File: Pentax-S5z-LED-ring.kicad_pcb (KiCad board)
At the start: 2 copper layers, 41.7 x 41.7 mm, 1 part

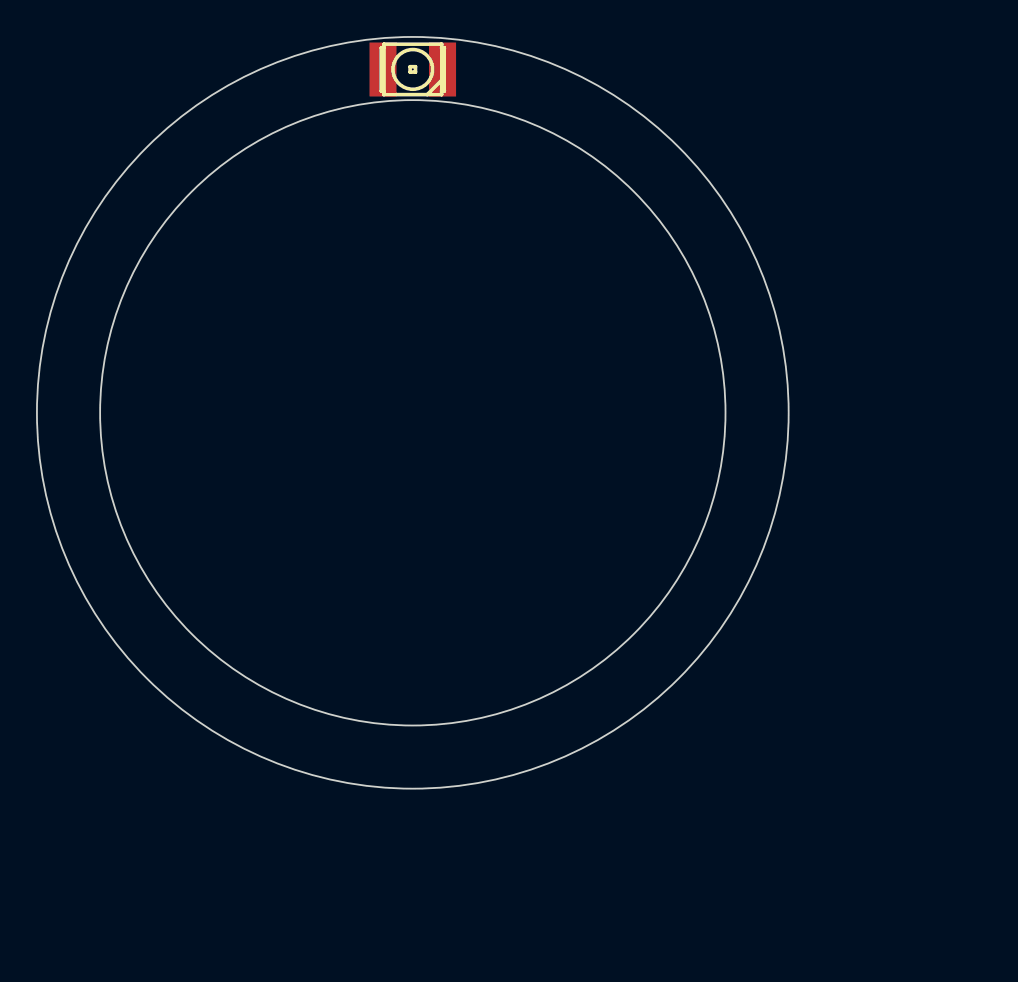
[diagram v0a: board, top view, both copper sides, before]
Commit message: First doodles.
Haven't decided yet how to drive the LEDs. Linear or switch-mode? Maybe
with 2x AAA cells + boost converter + ATtiny13 for PWM control.
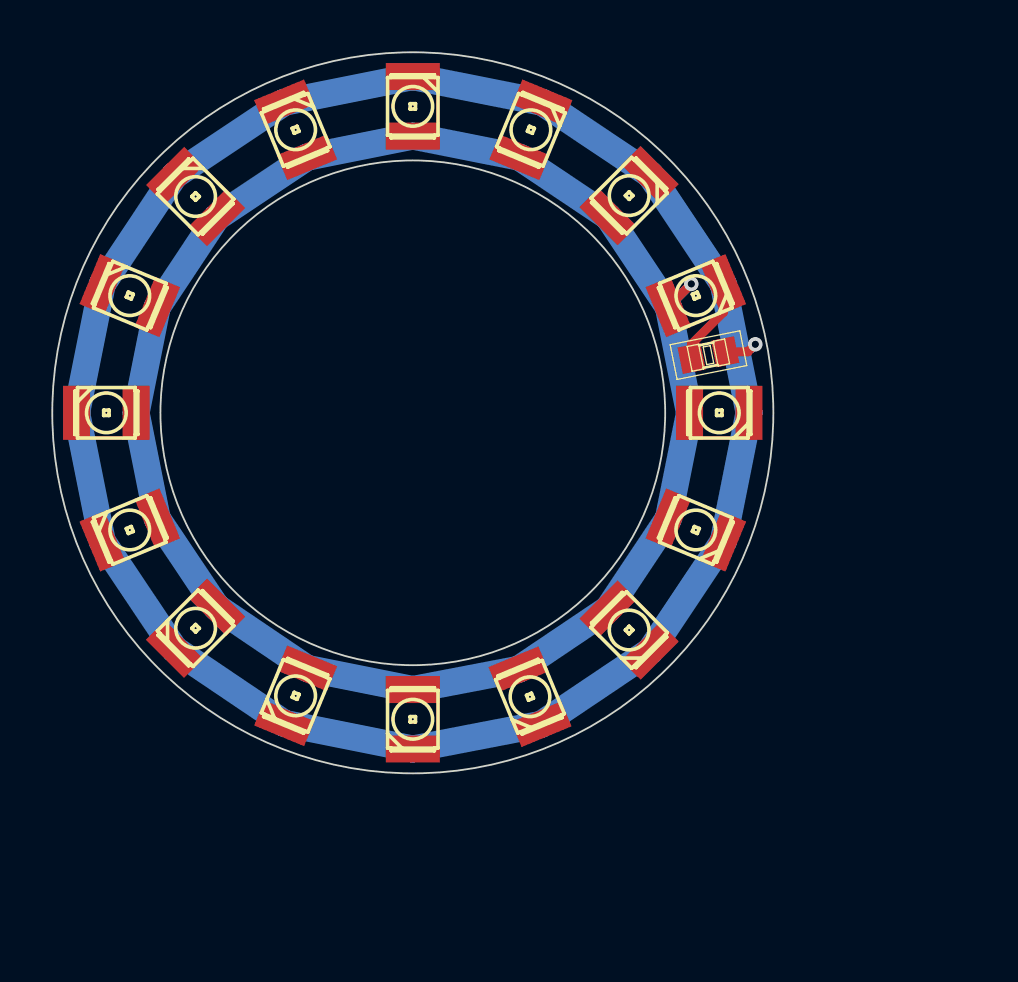
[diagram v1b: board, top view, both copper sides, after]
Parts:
- added >NAME: >VALUE, -R0805, F.Cu at (81.4, 61.8)
- added LED: VAL**, MADW__PLCC2, F.Cu at (80.7, 71.5)
- added LED: VAL**, MADW__PLCC2, F.Cu at (82.0, 65.0)
- added LED: VAL**, MADW__PLCC2, F.Cu at (48.0, 65.0)
- added LED: VAL**, MADW__PLCC2, F.Cu at (77.0, 53.0)
- added LED: VAL**, MADW__PLCC2, F.Cu at (53.0, 53.0)
- added LED: VAL**, MADW__PLCC2, F.Cu at (53.0, 77.0)
- added LED: VAL**, MADW__PLCC2, F.Cu at (77.0, 77.0)
- added LED: VAL**, MADW__PLCC2, F.Cu at (71.5, 49.3)
- added LED: VAL**, MADW__PLCC2, F.Cu at (49.3, 58.5)
- added LED: VAL**, MADW__PLCC2, F.Cu at (49.3, 71.5)
- added LED: VAL**, MADW__PLCC2, F.Cu at (80.7, 58.5)
- added LED: VAL**, MADW__PLCC2, F.Cu at (71.5, 80.8)
- added LED: VAL**, MADW__PLCC2, F.Cu at (58.5, 49.3)
- added LED: VAL**, MADW__PLCC2, F.Cu at (58.5, 80.7)
- added LED: VAL**, MADW__PLCC2, F.Cu at (65.0, 82.0)
- moved LED 2.05 mm to (65.0, 48.0), turned to 90 degrees
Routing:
- net (no net): track 0.00 -> 223.7 mm, vias 0 -> 2
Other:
- board size 41.7 x 41.7 mm -> 40 x 40 mm
- net class Default: clearance 0.254 -> 0.25; trace_width 0.254 -> 0.5; via_dia 0.889 -> 0.8; via_drill 0.635 -> 0.4
- rule pad_to_mask_clearance: 0.2 -> 0
- rule trace_clearance: 0.254 -> 0.25
- rule trace_min: 0.254 -> 0.25
- rule via_min_drill: 0.508 -> 0.4
- rule via_min_size: 0.889 -> 0.8

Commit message: Placed a few traces.
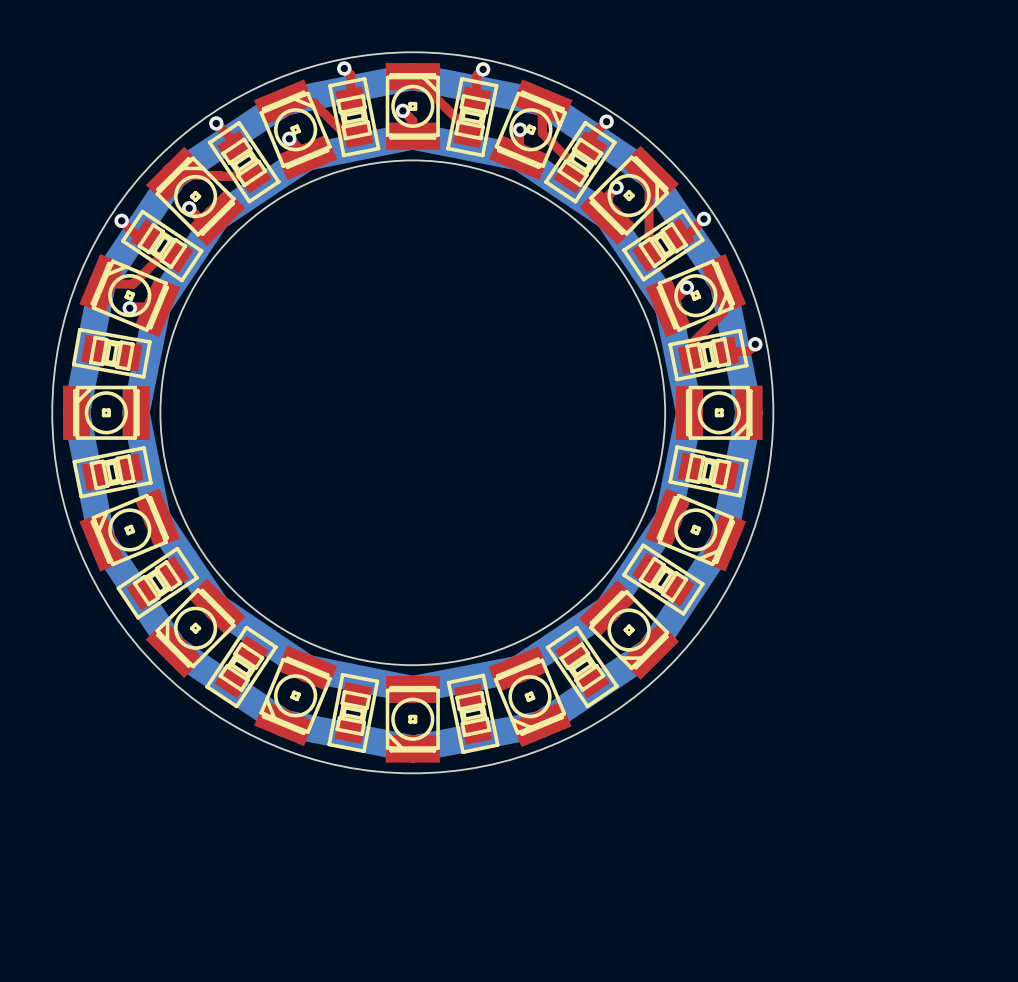
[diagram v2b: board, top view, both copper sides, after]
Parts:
- removed LED: VAL**, MADW__PLCC2
- added D3: LED, MADW__PLCC2-3528, F.Cu at (77.0, 53.0)
- added R1: 10R, MADW__R0805, F.Cu at (68.3, 48.6)
- added R10: 10R, MADW__R0805, F.Cu at (55.5, 79.1)
- added R11: 10R, MADW__R0805, F.Cu at (50.9, 74.5)
- added R12: 10R, MADW__R0805, F.Cu at (48.4, 68.3)
- added R13: 10R, MADW__R0805, F.Cu at (48.3, 61.7)
- added R14: 10R, MADW__R0805, F.Cu at (51.1, 55.8)
- added R15: 10R, MADW__R0805, F.Cu at (55.6, 51.1)
- added R16: 10R, MADW__R0805, F.Cu at (61.8, 48.6)
- added R2: 10R, MADW__R0805, F.Cu at (74.3, 51.1)
- added R3: 10R, MADW__R0805, F.Cu at (78.9, 55.7)
- added R5: 10R, MADW__R0805, F.Cu at (81.4, 68.2)
- added R6: 10R, MADW__R0805, F.Cu at (78.9, 74.2)
- added R7: 10R, MADW__R0805, F.Cu at (74.4, 79.1)
- added R8: 10R, MADW__R0805, F.Cu at (68.3, 81.7)
- added R9: 10R, MADW__R0805, F.Cu at (61.7, 81.7)
- D1, D2, D4, D5, D6, D7: renamed from LED; value VAL** -> LED; footprint MADW__PLCC2 -> MADW__PLCC2-3528
- D10, D11, D12, D13, D14, D15, D16, D8, D9: renamed from LED; value VAL** -> LED
- R4: renamed from >NAME; value >VALUE -> 10R; footprint -R0805 -> MADW__R0805
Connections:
- D1 pad 1: (no net) -> N-0000018
- D1 pad 2: (no net) -> N-000002
- D10 pad 1: (no net) -> N-0000018
- D10 pad 2: (no net) -> N-0000010
- D11 pad 1: (no net) -> N-0000018
- D11 pad 2: (no net) -> N-0000011
- D12 pad 1: (no net) -> N-0000018
- D12 pad 2: (no net) -> N-0000012
- D13 pad 1: (no net) -> N-0000018
- D13 pad 2: (no net) -> N-0000013
- D14 pad 1: (no net) -> N-0000018
- D14 pad 2: (no net) -> N-0000014
- D15 pad 1: (no net) -> N-0000018
- D15 pad 2: (no net) -> N-0000015
- D16 pad 1: (no net) -> N-0000018
- D16 pad 2: (no net) -> N-0000016
- D2 pad 1: (no net) -> N-0000018
- D2 pad 2: (no net) -> N-000003
- D4 pad 1: (no net) -> N-0000018
- D4 pad 2: (no net) -> N-000001
- D5 pad 1: (no net) -> N-0000018
- D5 pad 2: (no net) -> N-000005
- D6 pad 1: (no net) -> N-0000018
- D6 pad 2: (no net) -> N-000006
- D7 pad 1: (no net) -> N-0000018
- D7 pad 2: (no net) -> N-000007
- D8 pad 1: (no net) -> N-0000018
- D8 pad 2: (no net) -> N-000008
- D9 pad 1: (no net) -> N-0000018
- D9 pad 2: (no net) -> N-000009
- R4 pad 1: (no net) -> N-000001
- R4 pad 2: (no net) -> N-0000017
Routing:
- net (no net): track 223.7 -> 0.00 mm, vias 2 -> 0
- net N-0000017: track 0.00 -> 137.3 mm, vias 0 -> 7
- net N-0000018: track 0.00 -> 118.2 mm, vias 0 -> 7
- net N-000001: track 0.00 -> 4.84 mm
- net N-0000016: track 0.00 -> 4.79 mm
- net N-000003: track 0.00 -> 4.77 mm
- net N-0000014: track 0.00 -> 4.77 mm
- net N-000004: track 0.00 -> 4.47 mm
- net N-0000015: track 0.00 -> 4.42 mm
- net N-000002: track 0.00 -> 4.36 mm

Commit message: Tweaks.
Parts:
- moved R11 0.32 mm to (51.1, 74.2), turned to 213.9 degrees
- moved R8 0.32 mm to (68.2, 81.4), turned to 281.7 degrees
- moved R13 0.30 mm to (48.6, 61.8)
- moved R10 0.28 mm to (55.7, 78.9), turned to 236.5 degrees
- moved R12 0.25 mm to (48.6, 68.2), turned to 191.3 degrees
- moved R9 0.25 mm to (61.8, 81.4), turned to 259.1 degrees
- moved R7 0.11 mm to (74.3, 79.0), turned to 304.3 degrees
- turned R6 to 326.9 degrees
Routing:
- net N-0000018: track 118.2 -> 148.4 mm, vias 7 -> 16
- net N-0000017: track 137.3 -> 163.4 mm, vias 7 -> 16
- net N-000009: track 0.00 -> 4.71 mm
- net N-000008: track 0.00 -> 4.46 mm
- net N-0000013: track 0.00 -> 4.43 mm
- net N-0000010: track 0.00 -> 4.43 mm
- net N-0000012: track 0.00 -> 4.43 mm
- net N-000006: track 0.00 -> 4.42 mm
- net N-000005: track 0.00 -> 4.42 mm
- net N-0000011: track 0.00 -> 4.40 mm
- net N-000007: track 0.00 -> 4.35 mm

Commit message: Now I need a control board.
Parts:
- added 1PIN: -, 1pin, B.Cu at (46.7, 63.2)
- added 1PIN: +, 1pin, B.Cu at (50.2, 62.3)
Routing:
- net N-0000018: track 148.4 -> 147.5 mm

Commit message: Tweaks.
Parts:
- added mouse-bite-2mm: VAL**, MADW__mouse-bite-2mm-slot, F.Cu at (78.1, 65.0)
- added mouse-bite-2mm: VAL**, MADW__mouse-bite-2mm-slot, F.Cu at (51.9, 65.0)
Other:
- outline, holes or cut-outs redrawn
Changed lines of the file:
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@@
     (area 43.648616 44.422949 85.577051 85.577051)
     (thickness 1.6)
-    (drawings 2)
+    (drawings 24)
     (tracks 214)
     (zones 0)
-    (modules 34)
+    (modules 36)
     (nets 19)
   )
@@
     (add_net N-000009)
   )
+  (module MADW__mouse-bite-2mm-slot (layer F.Cu)
+    (at 78.1 65 270)
+    (fp_text reference mouse-bite-2mm (at 0 -2 270) (layer F.SilkS) hide
+      (effects (font (size 1 1) (thickness 0.2)))
+    )
+    (fp_text value VAL** (at 0 2.1 270) (layer F.SilkS) hide
+      (effects (font (size 1 1) (thickness 0.2)))
+    )
+    (pad "" np_thru_hole circle (at 0 -0.75 270) (size 0.5 0.5) (drill 0.5)
+      (layers *.Cu *.Mask F.SilkS)
+    )
+    (pad "" np_thru_hole circle (at 0 1.25 270) (size 0.5 0.5) (drill 0.5)
+      (layers *.Cu *.Mask F.SilkS)
+    )
+    (pad "" np_thru_hole circle (at 0.75 -0.75 270) (size 0.5 0.5) (drill 0.5)
+      (layers *.Cu *.Mask F.SilkS)
+    )
+    (pad "" np_thru_hole circle (at -0.75 -0.75 270) (size 0.5 0.5) (drill 0.5)
+      (layers *.Cu *.Mask F.SilkS)
+    )
+    (pad "" np_thru_hole circle (at -0.75 1.25 270) (size 0.5 0.5) (drill 0.5)
+      (layers *.Cu *.Mask F.SilkS)
+    )
+    (pad "" np_thru_hole circle (at 0.75 1.25 270) (size 0.5 0.5) (drill 0.5)
+      (layers *.Cu *.Mask F.SilkS)
+    )
+  )
+  (module MADW__mouse-bite-2mm-slot (layer F.Cu)
+    (at 51.9 65 90)
+    (fp_text reference mouse-bite-2mm (at 0 -2 90) (layer F.SilkS) hide
+      (effects (font (size 1 1) (thickness 0.2)))
+    )
+    (fp_text value VAL** (at 0 2.1 90) (layer F.SilkS) hide
+      (effects (font (size 1 1) (thickness 0.2)))
+    )
+    (pad "" np_thru_hole circle (at 0 -0.75 90) (size 0.5 0.5) (drill 0.5)
+      (layers *.Cu *.Mask F.SilkS)
+    )
+    (pad "" np_thru_hole circle (at 0 1.25 90) (size 0.5 0.5) (drill 0.5)
+      (layers *.Cu *.Mask F.SilkS)
+    )
+    (pad "" np_thru_hole circle (at 0.75 -0.75 90) (size 0.5 0.5) (drill 0.5)
+      (layers *.Cu *.Mask F.SilkS)
+    )
+    (pad "" np_thru_hole circle (at -0.75 -0.75 90) (size 0.5 0.5) (drill 0.5)
+      (layers *.Cu *.Mask F.SilkS)
+    )
+    (pad "" np_thru_hole circle (at -0.75 1.25 90) (size 0.5 0.5) (drill 0.5)
+      (layers *.Cu *.Mask F.SilkS)
+    )
+    (pad "" np_thru_hole circle (at 0.75 1.25 90) (size 0.5 0.5) (drill 0.5)
+      (layers *.Cu *.Mask F.SilkS)
+    )
+  )
   (module 1pin (layer B.Cu)
     (at 46.7 63.25 349)
@@
     )
   )
+  (gr_circle (center 65 65) (end 79 65) (layer F.SilkS) (width 0.2))
+  (gr_arc (start 65 65) (end 78.9 63.4) (angle -83.5) (layer Edge.Cuts) (width 0.1))
+  (gr_arc (start 65 65) (end 51.1 66.6) (angle -83.5) (layer Edge.Cuts) (width 0.1))
+  (gr_arc (start 65 65) (end 51.1 63.4) (angle 83.5) (layer Edge.Cuts) (width 0.1))
+  (gr_arc (start 65 65) (end 78.9 66.6) (angle 83.5) (layer Edge.Cuts) (width 0.1))
+  (gr_line (start 53.35 70) (end 76.65 70) (angle 90) (layer Edge.Cuts) (width 0.1))
+  (gr_line (start 53.35 60) (end 76.65 60) (angle 90) (layer Edge.Cuts) (width 0.1))
+  (gr_arc (start 52.35 63) (end 53.35 63) (angle 90) (layer Edge.Cuts) (width 0.1))
+  (gr_arc (start 51.7 63.4) (end 51.7 64) (angle 90) (layer Edge.Cuts) (width 0.1))
+  (gr_line (start 53.35 63) (end 53.35 60) (angle 90) (layer Edge.Cuts) (width 0.1))
+  (gr_line (start 53.35 67) (end 53.35 70) (angle 90) (layer Edge.Cuts) (width 0.1))
+  (gr_arc (start 51.7 66.6) (end 51.7 66) (angle -90) (layer Edge.Cuts) (width 0.1))
+  (gr_arc (start 52.35 67) (end 53.35 67) (angle -90) (layer Edge.Cuts) (width 0.1))
+  (gr_line (start 52.35 66) (end 51.7 66) (angle 90) (layer Edge.Cuts) (width 0.1))
+  (gr_line (start 52.35 64) (end 51.7 64) (angle 90) (layer Edge.Cuts) (width 0.1))
   (gr_circle (center 65 65) (end 85 65) (layer Edge.Cuts) (width 0.1))
-  (gr_circle (center 65 65) (end 79 65) (layer Edge.Cuts) (width 0.1))
+  (gr_line (start 77.65 66) (end 78.3 66) (angle 90) (layer Edge.Cuts) (width 0.1))
+  (gr_line (start 77.65 64) (end 78.3 64) (angle 90) (layer Edge.Cuts) (width 0.1))
+  (gr_arc (start 77.65 63) (end 76.65 63) (angle -90) (layer Edge.Cuts) (width 0.1))
+  (gr_arc (start 78.3 63.4) (end 78.3 64) (angle -90) (layer Edge.Cuts) (width 0.1))
+  (gr_line (start 76.65 63) (end 76.65 60) (angle 90) (layer Edge.Cuts) (width 0.1))
+  (gr_line (start 76.65 67) (end 76.65 70) (angle 90) (layer Edge.Cuts) (width 0.1))
+  (gr_arc (start 78.3 66.6) (end 78.3 66) (angle 90) (layer Edge.Cuts) (width 0.1))
+  (gr_arc (start 77.65 67) (end 76.65 67) (angle 90) (layer Edge.Cuts) (width 0.1))
   (segment (start 80.468455 61.986141) (end 82.224401 57.868572) (width 0.5) (layer F.Cu) (net 1) (status 30))
   (segment (start 56.224318 78.107842) (end 57.868572 82.224401) (width 0.5) (layer F.Cu) (net 2) (status 30))

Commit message: Trying to build a controller board.
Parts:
- added IC1: ATTINY13-S, MADW__SO8_200mil_wide, F.Cu at (59.1, 66.8)
- added JP1: MADW__AVR_ISP, pin_array_3x2, F.Cu at (68.3, 65.9)
- added Q1: MOSFET_N, SOT23, F.Cu at (74.1, 62.5)
- added R17: 150R, MADW__R0805, F.Cu at (75.2, 67.2)
- added R18: 100k, MADW__R0805, F.Cu at (72.9, 67.2)
- added SW1: SW_PUSH, SIL-2, F.Cu at (93.9, 93.2)
- added SW2: SW_PUSH, SIL-2, F.Cu at (87.8, 84.7)
- D10, D11, D12, D13, D14, D15, D16, D8, D9: footprint MADW__PLCC2 -> MADW__PLCC2-3528
- R1: value 10R -> 60R
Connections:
- D1 pad 1: N-0000018 (its old number) -> +5V
- D10 pad 1: N-0000018 (its old number) -> +5V
- D11 pad 1: N-0000018 (its old number) -> +5V
- D12 pad 1: N-0000018 (its old number) -> +5V
- D13 pad 1: N-0000018 (its old number) -> +5V
- D14 pad 1: N-0000018 (its old number) -> +5V
- D15 pad 1: N-0000018 (its old number) -> +5V
- D16 pad 1: N-0000018 (its old number) -> +5V
- D2 pad 1: N-0000018 (its old number) -> +5V
- D3 pad 1: N-0000018 (its old number) -> +5V
- D4 pad 1: N-0000018 (its old number) -> +5V
- D5 pad 1: N-0000018 (its old number) -> +5V
- D6 pad 1: N-0000018 (its old number) -> +5V
- D7 pad 1: N-0000018 (its old number) -> +5V
- D8 pad 1: N-0000018 (its old number) -> +5V
- D9 pad 1: N-0000018 (its old number) -> +5V
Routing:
- net N-0000018 (its old number): track 147.5 -> 0.00 mm, vias 16 -> 0
- net +5V: track 0.00 -> 147.5 mm, vias 0 -> 16

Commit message: Added proper SMD push-buttons.
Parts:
- JP1: value MADW__AVR_ISP -> ISP; footprint pin_array_3x2 -> MADW__PIN_ARRAY_3x2_2mm
- SW1, SW2: footprint SIL-2 -> MADW__push-button-SMD-3.7x6.0
- moved SW1 47.2 mm to (58.5, 61.9), turned to 180 degrees
- moved SW2 30.3 mm to (67.8, 61.9)
- moved JP1 1.61 mm to (68.2, 67.5), turned to 180 degrees

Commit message: ...
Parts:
- removed 1PIN: -, 1pin
- removed 1PIN: +, 1pin
- added P1: CONN_2, MADW__SIL-2, F.Cu at (70.5, 57.1)
- added P2: +, MADW__SIL-1, B.Cu at (49.5, 67.5)
- added P3: -, MADW__SIL-1, B.Cu at (47.5, 63.0)
- added P4: CONN_2, MADW__SIL-2, F.Cu at (59.5, 57.4)
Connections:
- D1 pad 1: +5V -> N-0000019
- D10 pad 1: +5V -> N-0000019
- D11 pad 1: +5V -> N-0000019
- D12 pad 1: +5V -> N-0000019
- D13 pad 1: +5V -> N-0000019
- D14 pad 1: +5V -> N-0000019
- D15 pad 1: +5V -> N-0000019
- D16 pad 1: +5V -> N-0000019
- D2 pad 1: +5V -> N-0000019
- D3 pad 1: +5V -> N-0000019
- D4 pad 1: +5V -> N-0000019
- D5 pad 1: +5V -> N-0000019
- D6 pad 1: +5V -> N-0000019
- D7 pad 1: +5V -> N-0000019
- D8 pad 1: +5V -> N-0000019
- D9 pad 1: +5V -> N-0000019
- Q1 pad 3: N-0000026 (its old number) -> N-0000010
- R1 pad 2: N-0000026 (its old number) -> N-0000011
- R10 pad 2: N-0000026 (its old number) -> N-0000011
- R11 pad 2: N-0000026 (its old number) -> N-0000011
- R12 pad 2: N-0000026 (its old number) -> N-0000011
- R13 pad 2: N-0000026 (its old number) -> N-0000011
- R14 pad 2: N-0000026 (its old number) -> N-0000011
- R15 pad 2: N-0000026 (its old number) -> N-0000011
- R16 pad 2: N-0000026 (its old number) -> N-0000011
- R2 pad 2: N-0000026 (its old number) -> N-0000011
- R3 pad 2: N-0000026 (its old number) -> N-0000011
- R4 pad 2: N-0000026 (its old number) -> N-0000011
- R5 pad 2: N-0000026 (its old number) -> N-0000011
- R6 pad 2: N-0000026 (its old number) -> N-0000011
- R7 pad 2: N-0000026 (its old number) -> N-0000011
- R8 pad 2: N-0000026 (its old number) -> N-0000011
- R9 pad 2: N-0000026 (its old number) -> N-0000011
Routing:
- net N-0000011: track 0.00 -> 172.8 mm, vias 0 -> 16
- net N-0000026 (its old number): track 163.3 -> 0.00 mm, vias 16 -> 0
- net N-0000019: track 0.00 -> 152.8 mm, vias 0 -> 16
- net +5V: track 147.5 -> 0.00 mm, vias 16 -> 0
